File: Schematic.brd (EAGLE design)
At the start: 84 x 96 mm, 64 parts

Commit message: finished routing
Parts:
- moved C6 2.29 mm to (18.4, 36.8)
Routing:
- net GND: track 112.1 -> 397.8 mm, vias 0 -> 9
- net N$16: track 6.75 -> 4.32 mm

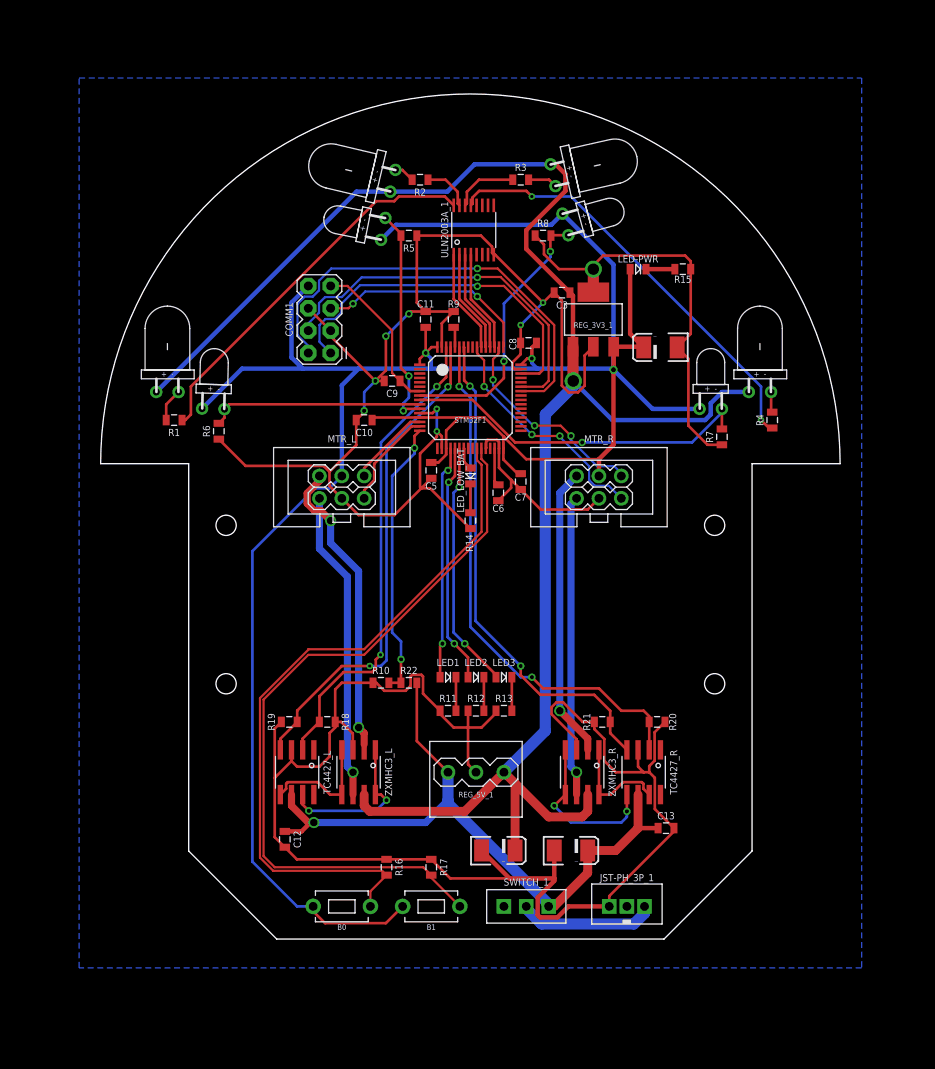
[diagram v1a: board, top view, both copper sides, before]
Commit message: Corrected GND plane connections
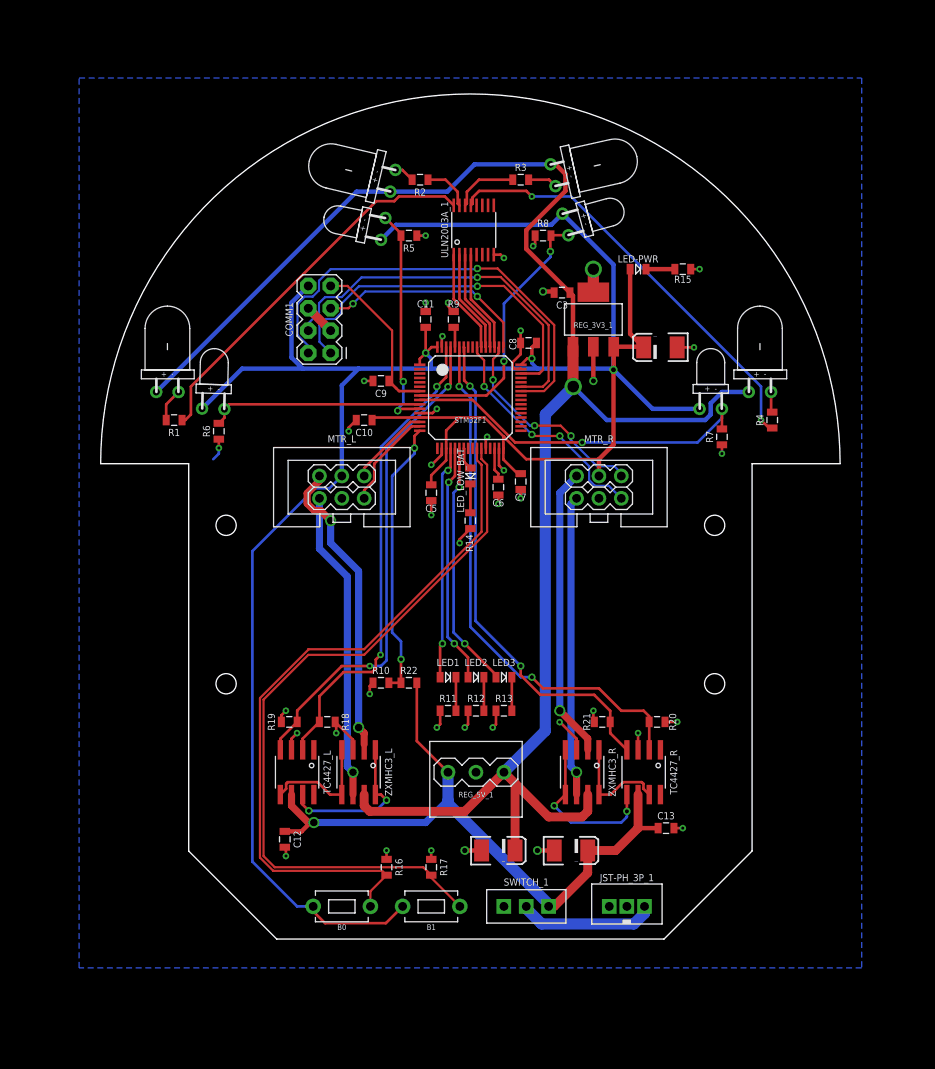
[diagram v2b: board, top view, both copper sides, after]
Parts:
- moved C5 2.54 mm to (10.8, 36.8)
- moved C9 1.27 mm to (5.08, 49.5)
- moved C6 0.64 mm to (18.4, 37.5)
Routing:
- net GND: track 397.8 -> 80.9 mm, vias 9 -> 41
- net +3V3: track 277.6 -> 279.6 mm
- net NRST: track 18.2 -> 19.8 mm
- net N$16: track 4.32 -> 3.69 mm

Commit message: Minor fix
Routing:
- net RE_RD: track 40.8 -> 41.9 mm
- net RPWM_B: track 57.0 -> 57.8 mm
- net +5V: track 197.2 -> 196.4 mm
- net RENC_B: track 26.7 -> 27.4 mm

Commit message: Fix errors
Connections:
- net +5V: no longer ZXMHC3_L.P1S/P2S, ZXMHC3_R.P1S/P2S
- net V+: now also ZXMHC3_L.P1S/P2S, ZXMHC3_R.P1S/P2S
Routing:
- net +5V: track 196.4 -> 165.1 mm
- net V+: track 77.6 -> 92.1 mm
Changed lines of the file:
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@@
 <grid distance="25" unitdist="mil" unit="mil" style="lines" multiple="1" display="yes" altdistance="5" altunitdist="mil" altunit="mil"/>
 <layers>
-<layer number="1" name="Top" color="4" fill="1" visible="no" active="yes"/>
+<layer number="1" name="Top" color="4" fill="1" visible="yes" active="yes"/>
 <layer number="2" name="Route2" color="16" fill="1" visible="no" active="no"/>
 <layer number="3" name="Route3" color="17" fill="1" visible="no" active="no"/>
@@
 <layer number="19" name="Unrouted" color="6" fill="1" visible="yes" active="yes"/>
 <layer number="20" name="Dimension" color="24" fill="1" visible="yes" active="yes"/>
-<layer number="21" name="tPlace" color="7" fill="1" visible="no" active="yes"/>
+<layer number="21" name="tPlace" color="7" fill="1" visible="yes" active="yes"/>
 <layer number="22" name="bPlace" color="7" fill="1" visible="yes" active="yes"/>
-<layer number="23" name="tOrigins" color="15" fill="1" visible="no" active="yes"/>
+<layer number="23" name="tOrigins" color="15" fill="1" visible="yes" active="yes"/>
 <layer number="24" name="bOrigins" color="15" fill="1" visible="yes" active="yes"/>
-<layer number="25" name="tNames" color="7" fill="1" visible="no" active="yes"/>
+<layer number="25" name="tNames" color="7" fill="1" visible="yes" active="yes"/>
 <layer number="26" name="bNames" color="7" fill="1" visible="yes" active="yes"/>
 <layer number="27" name="tValues" color="7" fill="1" visible="no" active="yes"/>
@@
 <layer number="37" name="tTest" color="7" fill="1" visible="no" active="yes"/>
 <layer number="38" name="bTest" color="7" fill="1" visible="no" active="yes"/>
-<layer number="39" name="tKeepout" color="4" fill="11" visible="no" active="yes"/>
+<layer number="39" name="tKeepout" color="4" fill="11" visible="yes" active="yes"/>
 <layer number="40" name="bKeepout" color="1" fill="11" visible="yes" active="yes"/>
-<layer number="41" name="tRestrict" color="4" fill="10" visible="no" active="yes"/>
+<layer number="41" name="tRestrict" color="4" fill="10" visible="yes" active="yes"/>
 <layer number="42" name="bRestrict" color="1" fill="10" visible="yes" active="yes"/>
 <layer number="43" name="vRestrict" color="2" fill="10" visible="no" active="yes"/>
@@
 <layer number="49" name="Reference" color="7" fill="1" visible="no" active="yes"/>
 <layer number="50" name="dxf" color="7" fill="1" visible="no" active="no"/>
-<layer number="51" name="tDocu" color="7" fill="1" visible="no" active="yes"/>
+<layer number="51" name="tDocu" color="7" fill="1" visible="yes" active="yes"/>
 <layer number="52" name="bDocu" color="7" fill="1" visible="yes" active="yes"/>
 <layer number="53" name="tGND_GNDA" color="7" fill="9" visible="no" active="no"/>
@@
 <contactref element="C2" pad="A"/>
 <contactref element="REG_3V3_1" pad="IN"/>
-<contactref element="ZXMHC3_L" pad="P1S/P2S"/>
-<contactref element="ZXMHC3_R" pad="P1S/P2S"/>
-<wire x1="24.13" y1="0" x2="27.94" y2="0" width="1.016" layer="1"/>
-<wire x1="27.94" y1="0" x2="28.575" y2="0.635" width="1.016" layer="1"/>
-<wire x1="28.575" y1="0.635" x2="28.575" y2="2.54" width="1.016" layer="1"/>
-<wire x1="19.05" y1="5.08" x2="14.605" y2="0.635" width="1.016" layer="1"/>
-<wire x1="14.605" y1="0.635" x2="3.81" y2="0.635" width="1.016" layer="1"/>
-<wire x1="3.81" y1="0.635" x2="3.175" y2="1.27" width="1.016" layer="1"/>
-<wire x1="3.175" y1="1.27" x2="3.175" y2="2.54" width="1.016" layer="1"/>
 <wire x1="20.315" y1="-3.81" x2="20.315" y2="3.815" width="1.016" layer="1"/>
 <wire x1="19.05" y1="5.08" x2="23.749" y2="9.779" width="1.27" layer="16"/>
@@
 <wire x1="24.92215625" y1="74.13784375" x2="24.348865625" y2="74.13784375" width="0.508" layer="1"/>
 <wire x1="19.05" y1="5.08" x2="20.315" y2="3.815" width="1.016" layer="1"/>
-<wire x1="20.315" y1="3.815" x2="24.13" y2="0" width="1.016" layer="1"/>
 </signal>
 <signal name="V+">
@@
 <wire x1="34.29" y1="-1.265" x2="34.285" y2="-1.27" width="1.016" layer="1"/>
 <wire x1="34.29" y1="2.54" x2="34.29" y2="-1.265" width="1.016" layer="1"/>
+<contactref element="ZXMHC3_L" pad="P1S/P2S"/>
+<contactref element="ZXMHC3_R" pad="P1S/P2S"/>
+<wire x1="3.175" y1="2.54" x2="3.175" y2="0.635" width="0.8128" layer="1"/>
+<wire x1="3.175" y1="0.635" x2="1.905" y2="-0.635" width="0.8128" layer="1"/>
+<wire x1="1.905" y1="-0.635" x2="-2.54" y2="-0.635" width="0.8128" layer="1"/>
+<wire x1="28.575" y1="2.54" x2="28.575" y2="-3.805" width="0.8128" layer="1"/>
+<wire x1="28.575" y1="-3.805" x2="28.57" y2="-3.81" width="0.8128" layer="1"/>
 </signal>
 <signal name="N$9">

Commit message: finished routing
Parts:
- C2: value 47 -> 47uF
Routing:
- net V+: track 92.1 -> 88.1 mm, vias 1 -> 0
- net N$4: track 48.7 -> 51.0 mm
- net +3V3: track 279.6 -> 277.6 mm
- net RPWM_B: track 57.8 -> 56.0 mm
- net RE_RD: track 41.9 -> 40.3 mm, vias 1 -> 2
- net GND: track 80.9 -> 79.4 mm
- net RPWM_A: track 60.7 -> 59.5 mm
- net VOLTMETER: track 31.7 -> 30.9 mm
- net LPWM_A: track 54.4 -> 55.2 mm

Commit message: 03022020 meeting
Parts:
- moved RE_LF 2.62 mm to (2.79, 67.4), turned to 80 degrees
- moved EM_2 2.01 mm to (4.57, 73.0), turned to 80 degrees
- moved RE_RD 1.14 mm to (43.7, 46.4), turned to 357 degrees
- moved EM_4 0.64 mm to (48.9, 48.3), turned to 357 degrees
- turned EM_1 to 3 degrees
- turned EM_3 to 280 degrees
- turned RE_LD to 3 degrees
- turned RE_RF to 280 degrees
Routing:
- net RE_LF: track 25.6 -> 29.2 mm
- net +3V3: track 277.6 -> 280.7 mm
- net N$6: track 2.36 -> 4.59 mm
- net N$1: track 43.7 -> 44.8 mm
- net N$4: track 51.0 -> 51.9 mm

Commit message: generated gerber files
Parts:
- moved R18 1.27 mm to (-1.02, 12.1)
